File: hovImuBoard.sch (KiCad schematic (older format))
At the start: 67 parts, among them J1 AVR-ISP-6, J2 Ext. Power, J3 54602-908LF, J4 AVR-JTAG-10, J5 ExtensionPort, J6 Debug, U1 LD2981, U2 BMX160, U3 SN65HVD32DR, U4 ATmega1284P-AU, U5 TPS62173DSG, U6 TPS62172DSG

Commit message: WIP: Redesign of the sensor board.
Major re-design:
- LVDS instead of RS422 driver
- Simplify buck converter design.
- Make the back-plane mostly un-interrupted.
- Smaller cpacitors, eliminate tantal capacitors.
- Make ESD diode smaller.
- Pick different parts.
- Smaller LEDs.
- Eliminate the diodes at the buck converters.
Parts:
- removed C11, C13, C14: 47uF, Capacitor_Tantalum_SMD:CP_EIA-7343-31_Kemet-D, symbol Device:CP
- removed C15, C19, C20, C24, C4: 220nF, Capacitor_SMD:C_0805_2012Metric, symbol Device:C
- removed D4, D5: B120-E3, Diode_SMD:D_SMA, symbol Diode:B120-E3
- added C11, C13, C14: 22uF, Capacitor_SMD:C_1210_3225Metric, symbol Device:C
- added JP1: SolderJumper_2_Bridged, Jumper:SolderJumper-2_P1.3mm_Bridged2Bar_Pad1.0x1.5mm, symbol Jumper:SolderJumper_2_Bridged
- added R10: 100k, Resistor_SMD:R_0603_1608Metric, symbol Device:R
- added R11, R12: 47, Resistor_SMD:R_0603_1608Metric, symbol Device:R
- C1, C2: value 220nF -> 100nF; footprint Capacitor_SMD:C_0805_2012Metric -> Capacitor_SMD:C_0603_1608Metric; Description (none) -> CAP CER 0.1UF 25V X7R 0603 Non-magnetic; Digi-Key_PN 1276-6478-1-ND -> 1608-1295-1-ND; MPN CL21B224KBFNNNG -> 060330160104JXT; Manufacturer Samsung Electro-Mechanics -> Knowles Syfer
- C10, C25, C26, C27, C6, C7: value 220nF -> 100nF; footprint Capacitor_SMD:C_0805_2012Metric -> Capacitor_SMD:C_0603_1608Metric; Description (none) -> CAP CER 0.1UF 25V X7R 0603; Digi-Key_PN 1276-6478-1-ND -> 311-1341-1-ND; MPN CL21B224KBFNNNG -> CC0603KRX7R8BB104; Manufacturer Samsung Electro-Mechanics -> Yageo
- C12: value 10uF -> 4.7uF; footprint Capacitor_SMD:C_1210_3225Metric -> Capacitor_SMD:C_1206_3216Metric; Description (none) -> CAP CER 4.7UF 25V X7R 1206; Digi-Key_PN 1276-1804-1-ND -> 399-8204-1-ND; MPN CL31B106KAHNNNE -> C1206C475K3RACTU; Manufacturer Samsung Electro-Mechanics -> KEMET
- C16, C21: Description (none) -> CAP CER 22UF 25V X7R 1210
- C3: value 220nF -> 4.7uF; footprint Capacitor_SMD:C_0805_2012Metric -> Capacitor_SMD:C_1206_3216Metric; Description (none) -> CAP CER 4.7UF 25V X7R 1206; Digi-Key_PN 1276-6478-1-ND -> 399-8204-1-ND; MPN CL21B224KBFNNNG -> C1206C475K3RACTU; Manufacturer Samsung Electro-Mechanics -> KEMET
- C5: value 2.2uF -> 4.7uF; footprint Capacitor_SMD:C_0805_2012Metric -> Capacitor_SMD:C_1206_3216Metric; Description (none) -> CAP CER 4.7UF 25V X7R 1206; Digi-Key_PN 1276-2953-1-ND -> 399-8204-1-ND; MPN CL21B225KAFNFNE -> C1206C475K3RACTU; Manufacturer Samsung Electro-Mechanics -> KEMET
- C8, C9: footprint Capacitor_SMD:C_0805_2012Metric -> Capacitor_SMD:C_0603_1608Metric; Description (none) -> CAP CER 20PF 50V C0G/NPO 0603; Digi-Key_PN 1276-1829-1-ND -> 311-1424-1-ND; MPN CL21C200JBANNNC -> CC0603JRNPO9BN200; Manufacturer Samsung Electro-Mechanics -> Yageo
- D1, D2: value LED_Dual_ACA -> LED Green/Red; footprint LED_THT:LED_D5.0mm-3 -> hovImuBoard:LED_APHB1608LZGKSURKC; symbol Device:LED_Dual_ACA -> Device:LED_Dual_ACAC; Description (none) -> LED GREEN/RED CLEAR 4SMD
- D3: value P6SMB18A -> VESD16C1-02V-G3-08; footprint Diode_SMD:D_SMB -> Diode_SMD:D_SOD-523; Description (none) -> ESD PROTECTION DIODE 17V 6.3A SOD-523; Digi-Key_PN P6SMB18A-E3/52GICT-ND -> VESD16C1-02V-G3-08GICT-ND; MPN P6SMB18A-E3/52 -> VESD16C1-02V-G3-08
- J1: symbol Connector:AVR-ISP-6 -> hovImuBoard-rescue:AVR-ISP-6-Connector; Description (none) -> TE_1761681-1
- J2: Description (none) -> PinHeader1x02 P2.54mm Vertical
- J4: symbol Connector:AVR-JTAG-10 -> hovImuBoard-rescue:AVR-JTAG-10-Connector; Description (none) -> SHF-105-01-L-D-TH
- JP17: footprint Jumper:SolderJumper-2_P1.3mm_Open_Pad1.0x1.5mm -> Jumper:SolderJumper-2_P1.3mm_Open_RoundedPad1.0x1.5mm
- JP18: footprint Jumper:SolderJumper-2_P1.3mm_Bridged_Pad1.0x1.5mm -> Jumper:SolderJumper-2_P1.3mm_Bridged_RoundedPad1.0x1.5mm
- L1: value 100nH -> 240nH; footprint Inductor_SMD:L_0402_1005Metric -> Inductor_SMD:L_0805_2012Metric; Description (none) -> FIXED IND 240NH 2.4A 50 MOHM; Digi-Key_PN 587-6430-1-ND -> 490-15988-1-ND; MPN MCEE1005TR10MHN -> LQM21PNR24MEHD; Manufacturer Taiyo Yuden -> Murata Electronics
- L2: value 470nH -> 1.2uH; footprint Inductor_SMD:L_Taiyo-Yuden_NR-20xx -> hovImuBoard:IND_1231AS-H-1R2N=P3; Description (none) -> FIXED IND 1.2UH 2.9A 36 MOHM; Digi-Key_PN 587-4289-1-ND -> 490-14180-1-ND; MPN NRV2010TR47NGF -> 1231AS-H-1R2N=P3; Manufacturer Taiyo Yuden -> Murata Electronics
- L3: value 3.3uH -> 8.2uH; footprint Inductor_SMD:L_Taiyo-Yuden_NR-40xx -> Inductor_SMD:L_1812_4532Metric; Description (none) -> FIXED IND 8.2UH 1.3A 128 MOHM; Digi-Key_PN 587-2892-1-ND -> 490-16860-1-ND; MPN NRS4018T3R3MDGJ -> LQH43PN8R2M26L; Manufacturer Taiyo Yuden -> Murata Electronics
- L4, L5: footprint hovImuBoard:NRS5040T220MMGKV -> hovImuBoard:IND_LQH3NPN2R2MMEL; Description (none) -> FIXED IND 2.2UH 2.1A 78 MOHM; Digi-Key_PN 587-2552-1-ND -> 490-15950-1-ND; MPN NRS5012T2R2MMGF -> LQH3NPN2R2MMEL; Manufacturer Taiyo Yuden -> Murata Electronics
- R2, R5: value 200 -> 330; footprint Resistor_SMD:R_0805_2012Metric -> Resistor_SMD:R_0603_1608Metric; Description (none) -> RES SMD 330 OHM 1% 1/10W 0603; Digi-Key_PN 541-200CCT-ND -> P330HCT-ND; MPN CRCW0805200RFKEA -> ERJ-3EKF3300V; Manufacturer Vishay Dale -> Panasonic Electronic Components
- R3, R7: value 200 -> 787; footprint Resistor_SMD:R_0805_2012Metric -> Resistor_SMD:R_0603_1608Metric; Description (none) -> RES SMD 787 OHM 1% 1/10W 0603; Digi-Key_PN 541-200CCT-ND -> P787HCT-ND; MPN CRCW0805200RFKEA -> ERJ-3EKF7870V; Manufacturer Vishay Dale -> Panasonic Electronic Components
- R4: value 110m -> 180m; Description (none) -> RES 0.18 OHM 1% 1/2W 0805; Digi-Key_PN RCWE.11CCT-ND -> P19314CT-ND; MPN RCWE0603R110FKEA -> ERJ-6DSFR18V; Manufacturer Vishay Dale -> Panasonic Electronic Components
- R6: value 150 -> 100; footprint Resistor_SMD:R_0805_2012Metric -> Resistor_SMD:R_0603_1608Metric; Description (none) -> RES SMD 100 OHM 1% 1/4W 0603; Digi-Key_PN 541-150CCT-ND -> P100BYCT-ND; MPN CRCW0805150RFKEA -> ERJ-PA3F1000V; Manufacturer Vishay Dale -> Panasonic Electronic Components
- R8, R9: footprint Resistor_SMD:R_0805_2012Metric -> Resistor_SMD:R_0603_1608Metric; Description (none) -> RES SMD 4.7K OHM 1% 1/10W 0603; Digi-Key_PN 541-4.70KCCT-ND -> P4.70KHCT-ND; MPN CRCW08054K70FKEA -> ERJ-3EKF4701V; Manufacturer Vishay Dale -> Panasonic Electronic Components
- U3: value SN65HVD32DR -> SN65LVDS179DR; footprint Package_SO:SO-8_3.9x4.9mm_P1.27mm -> Package_SO:SOIC-8_3.9x4.9mm_P1.27mm; Description (none) -> LVDS TRANSCEIVER FULL 1/1 8SOIC; Digi-Key_PN 296-19627-1-ND -> 296-46329-1-ND; MPN SN65HVD32DR -> SN65LVDS179DR
- U5: Description (none) -> IC REG BUCK 5V 500MA 8WSON
- U6: Description (none) -> IC REG BUCK 3.3V 500MA 8WSON
- XTAL1: Description (none) -> CRYSTAL 9.2160MHZ 20PF SMD
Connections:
- wire segments 193 -> 179
- no-connect marks 22 -> 21
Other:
- note added: "LVDS transceiver"
- note removed: "RS-422 transceiver"
- moved on the sheet: C1, JP17, JP18, R6, S1, TP3, TP4

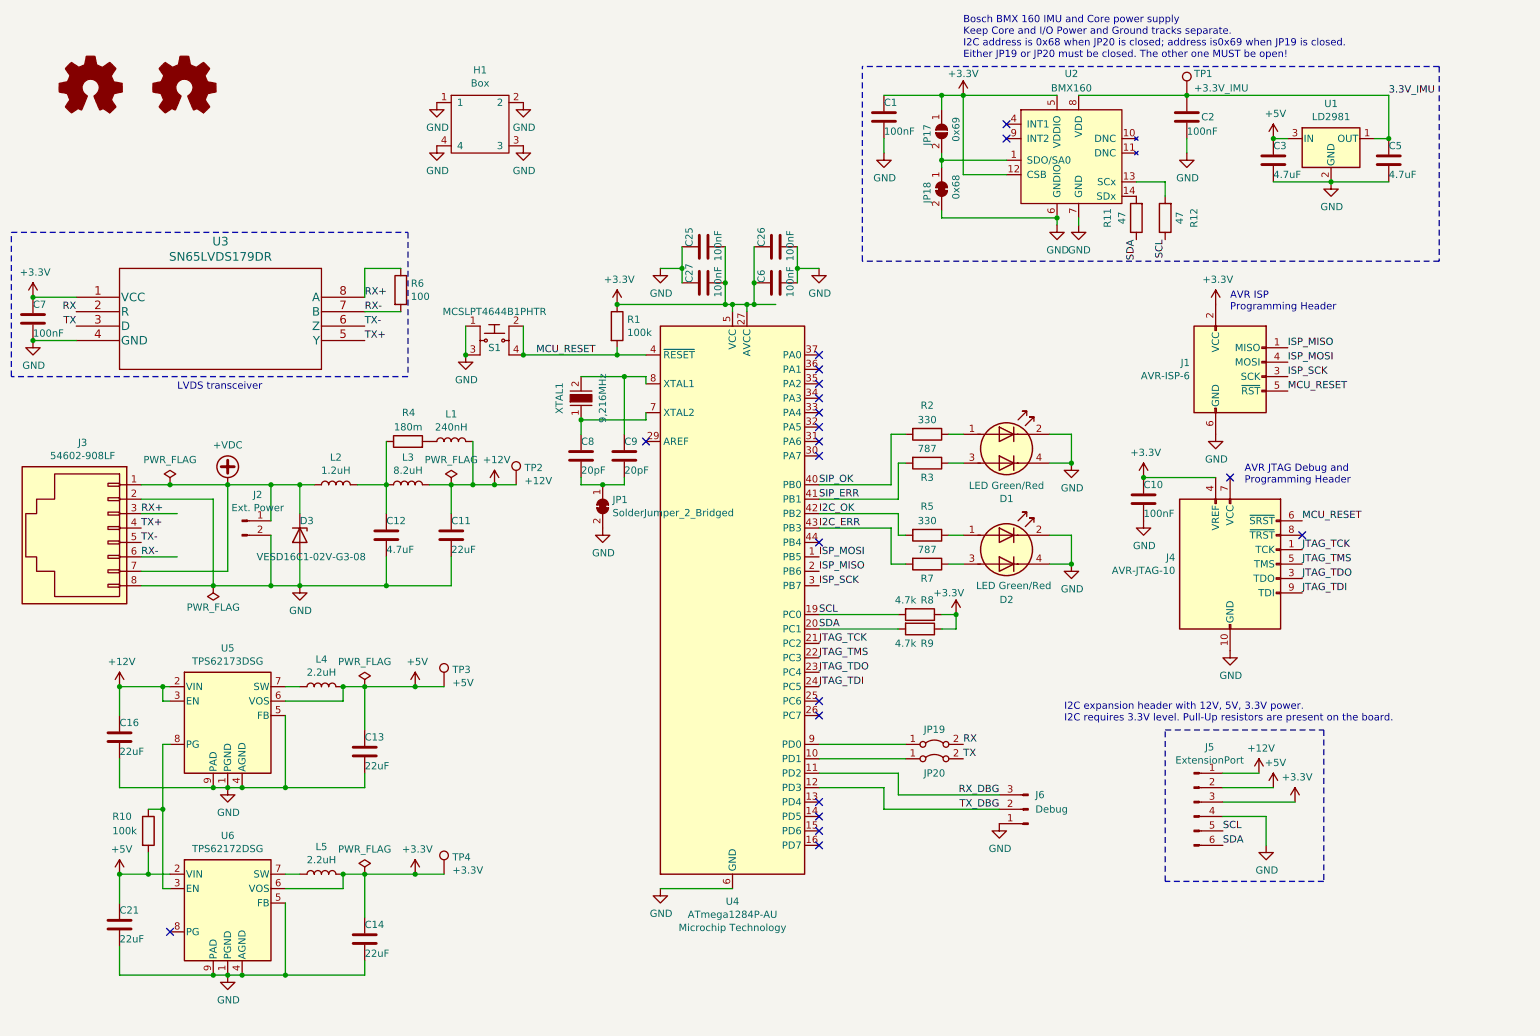
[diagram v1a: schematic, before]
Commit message: Complete re-design of hovImuBoard
- Create a proper local ground plane for the oscillator
- Create a local ground plane for the analog and digital ground.
- Clean separation of VDD and VDDIO, and ground lines for I/O.
- Hook up INT1 of the IMU with pin 15 of the MCU
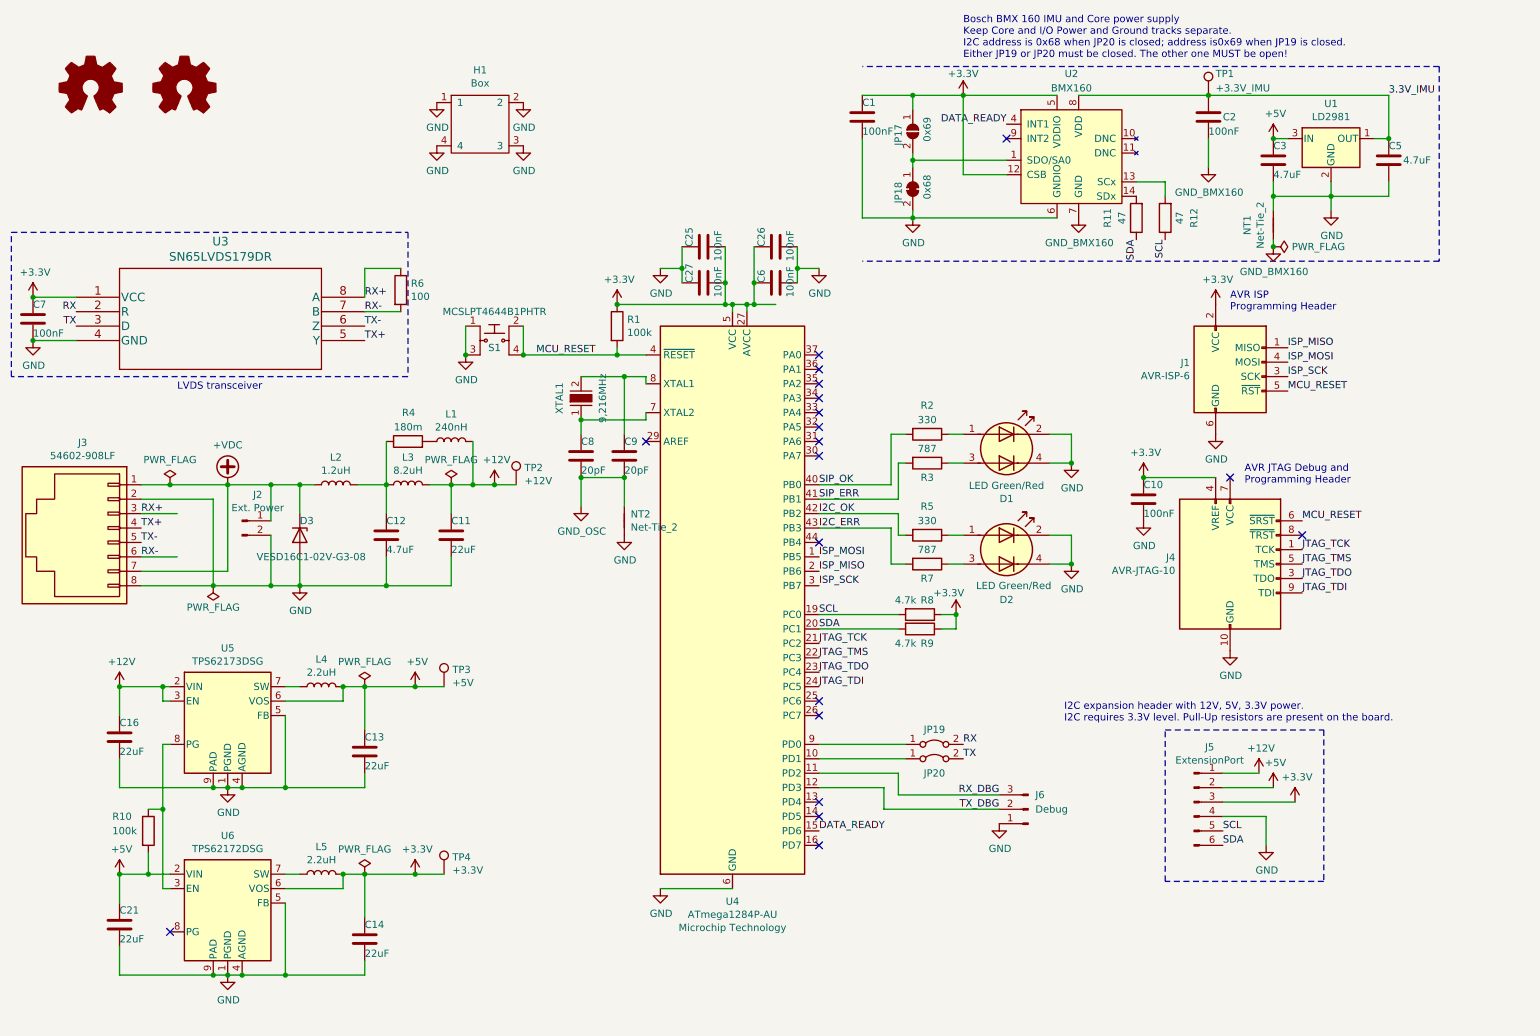
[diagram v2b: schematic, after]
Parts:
- removed JP1: SolderJumper_2_Bridged, Jumper:SolderJumper-2_P1.3mm_Bridged2Bar_Pad1.0x1.5mm, symbol Jumper:SolderJumper_2_Bridged
- added NT1: Net-Tie_2, NetTie:NetTie-2_SMD_Pad2.0mm, symbol Device:Net-Tie_2
- added NT2: Net-Tie_2, NetTie:NetTie-2_SMD_Pad0.5mm, symbol Device:Net-Tie_2
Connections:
- net GND: now also NT1.2, NT2.2; no longer C2.1, U2.2 (GND), U2.3 (GND), U2.7 (GND)
- net DATA_READY: now reaches U4.15 (PD6)
- net DATA_READY: now also U2.4 (INT1)
- net GND_OSC: now reaches C8.1, C9.1
- net GND_OSC: now also NT2.1
- new net GND_BMX160: C2.1, NT1.1, U2.2 (GND), U2.3 (GND), U2.7 (GND)
- no-connect marks 21 -> 19
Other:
- moved on the sheet: C1, C2, JP17, JP18, TP1

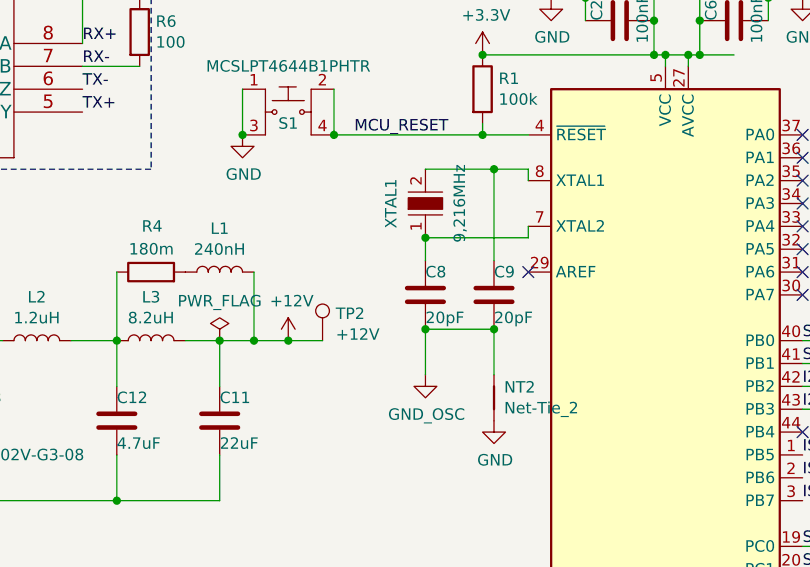
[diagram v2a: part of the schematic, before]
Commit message: Rev. is 0.3, minor trace optimiztions.
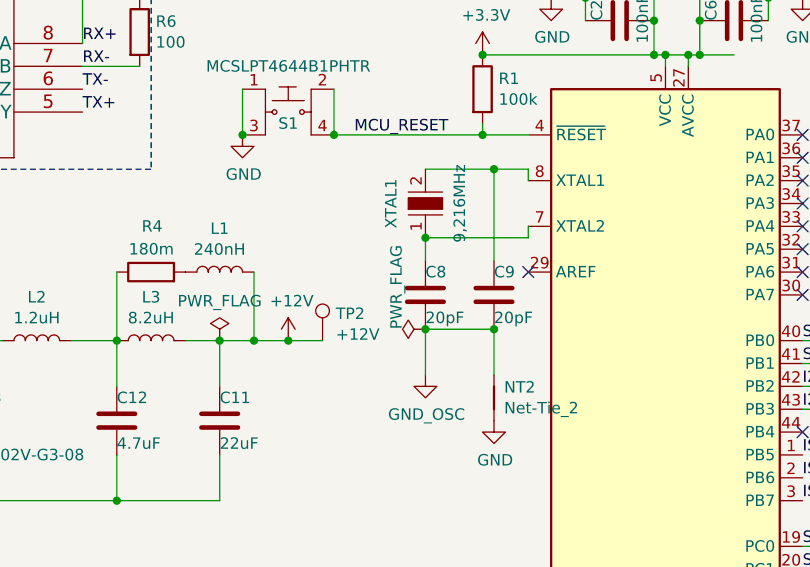
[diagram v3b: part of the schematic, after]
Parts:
- D1, D2: Digi-Key_PN 516-3048-1-ND -> 754-1955-1-ND; MPN HLMP-4000#002 -> APHB1608LZGKSURKC; Manufacturer Broadcom Limited -> Kingbright
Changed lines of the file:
@@
 F 1 "LED Green/Red" H 8100 3244 50  0000 C CNN
 F 2 "hovImuBoard:LED_APHB1608LZGKSURKC" H 8100 3500 50  0001 C CNN
-F 3 "https://docs.broadcom.com/docs/AV02-1552EN" H 8100 3500 50  0001 C CNN
-F 4 "516-3048-1-ND" H 8100 3500 50  0001 C CNN "Digi-Key_PN"
-F 5 "HLMP-4000#002" H 8100 3500 50  0001 C CNN "MPN"
-F 6 "Broadcom Limited" H 8100 3500 50  0001 C CNN "Manufacturer"
+F 3 "http://www.kingbrightusa.com/images/catalog/SPEC/APHB1608LZGKSURKC.pdf" H 8100 3500 50  0001 C CNN
+F 4 "754-1955-1-ND" H 8100 3500 50  0001 C CNN "Digi-Key_PN"
+F 5 "APHB1608LZGKSURKC" H 8100 3500 50  0001 C CNN "MPN"
+F 6 "Kingbright" H 8100 3500 50  0001 C CNN "Manufacturer"
 F 7 "LED GREEN/RED CLEAR 4SMD" H 8100 3500 50  0001 C CNN "Description"
 	1    8100 3500
@@
 F 1 "LED Green/Red" H 8150 3950 50  0000 C CNN
 F 2 "hovImuBoard:LED_APHB1608LZGKSURKC" H 8100 4200 50  0001 C CNN
-F 3 "https://docs.broadcom.com/docs/AV02-1552EN" H 8100 4200 50  0001 C CNN
-F 4 "516-3048-1-ND" H 8100 4200 50  0001 C CNN "Digi-Key_PN"
-F 5 "HLMP-4000#002" H 8100 4200 50  0001 C CNN "MPN"
-F 6 "Broadcom Limited" H 8100 4200 50  0001 C CNN "Manufacturer"
+F 3 "http://www.kingbrightusa.com/images/catalog/SPEC/APHB1608LZGKSURKC.pdf" H 8100 4200 50  0001 C CNN
+F 4 "754-1955-1-ND" H 8100 4200 50  0001 C CNN "Digi-Key_PN"
+F 5 "APHB1608LZGKSURKC" H 8100 4200 50  0001 C CNN "MPN"
+F 6 "Kingbright" H 8100 4200 50  0001 C CNN "Manufacturer"
 F 7 "LED GREEN/RED CLEAR 4SMD" H 8100 4200 50  0001 C CNN "Description"
 	1    8100 4200
@@
 	10650 1350 10750 1350
 Connection ~ 10750 1350
+$Comp
+L power:PWR_FLAG #FLG0104
+U 1 1 5F08E807
+P 5150 3700
+F 0 "#FLG0104" H 5150 3775 50  0001 C CNN
+F 1 "PWR_FLAG" H 5150 3827 50  0000 L CNN
+F 2 "" H 5150 3700 50  0001 C CNN
+F 3 "~" H 5150 3700 50  0001 C CNN
+	1    5150 3700
+	0    -1   -1   0
+$EndComp
 $EndSCHEMATC

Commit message: Remove one power symbol
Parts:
- J3: symbol hovImuBoard:54602-908LF -> hovImuBoard:RJ-45-hovIMUBoard-DCE-Board
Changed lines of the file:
@@
-$EndComp
-$Comp
-L power:PWR_FLAG #FLG03
-U 1 1 5D4F984A
-P 2600 4450
-F 0 "#FLG03" H 2600 4525 50  0001 C CNN
-F 1 "PWR_FLAG" H 2600 4600 50  0000 C CNN
-F 2 "" H 2600 4450 50  0001 C CNN
-F 3 "~" H 2600 4450 50  0001 C CNN
-	1    2600 4450
-	-1   0    0    1
 $EndComp
 $Comp
@@
 Wire Wire Line
 	2100 3850 2600 3850
-Wire Wire Line
-	2100 3750 2300 3750
-$Comp
-L hovImuBoard:54602-908LF J3
+$Comp
+L hovImuBoard:RJ-45-hovIMUBoard-DCE-Board J3
 U 1 1 5D4B7457
 P 1700 4050
@@
 	0    1    1    0
 $EndComp
-$Comp
-L power:PWR_FLAG #FLG01
-U 1 1 5D9E0353
-P 2300 3750
-F 0 "#FLG01" H 2300 3825 50  0001 C CNN
-F 1 "PWR_FLAG" H 2300 3923 50  0000 C CNN
-F 2 "" H 2300 3750 50  0001 C CNN
-F 3 "~" H 2300 3750 50  0001 C CNN
-	1    2300 3750
-	1    0    0    -1
-$EndComp
-Connection ~ 2300 3750
-Wire Wire Line
-	2300 3750 2700 3750
 Wire Notes Line
 	9200 5450 10300 5450
@@
 	0    -1   -1   0
 $EndComp
+Wire Wire Line
+	2100 3750 2700 3750
 $EndSCHEMATC

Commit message: Update KiCad, and libraries
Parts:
- H1: symbol hovImuBoard:Box -> hovImuBoard-rescue:Box-hovImuBoard
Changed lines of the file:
@@
 TX_DBG
 $Comp
-L hovImuBoard:Box H1
+L hovImuBoard-rescue:Box-hovImuBoard H1
 U 1 1 5D76E284
 P 4450 1250
@@
 Wire Wire Line
 	7100 1050 7450 1050
-Text Label 8100 1250 2    50   ~ 0
-DATA_READY
-Text Label 6800 6150 0    50   ~ 0
-DATA_READY
 $Comp
 L Jumper:SolderJumper_2_Bridged JP18
@@
 Wire Wire Line
 	2100 3750 2700 3750
+Text GLabel 8100 1250 0    50   Input ~ 0
+DATA_READY
+Text GLabel 6800 6150 2    50   Input ~ 0
+DATA_READY
 $EndSCHEMATC
